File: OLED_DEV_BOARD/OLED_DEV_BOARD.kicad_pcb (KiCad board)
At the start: 2 copper layers, 32 parts, among them J1 Barrel_Jack, J2 Conn_02x10_Odd_Even, J3 AudioJack3_Ground, J4 Conn_02x20_Odd_Even, SW1 SW_DIP_x02, SW2 SW_MEC_5E, SW3 SW_MEC_5E, SW4 SW_MEC_5E, SW5 SW_MEC_5E, SW6 SW_MEC_5E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

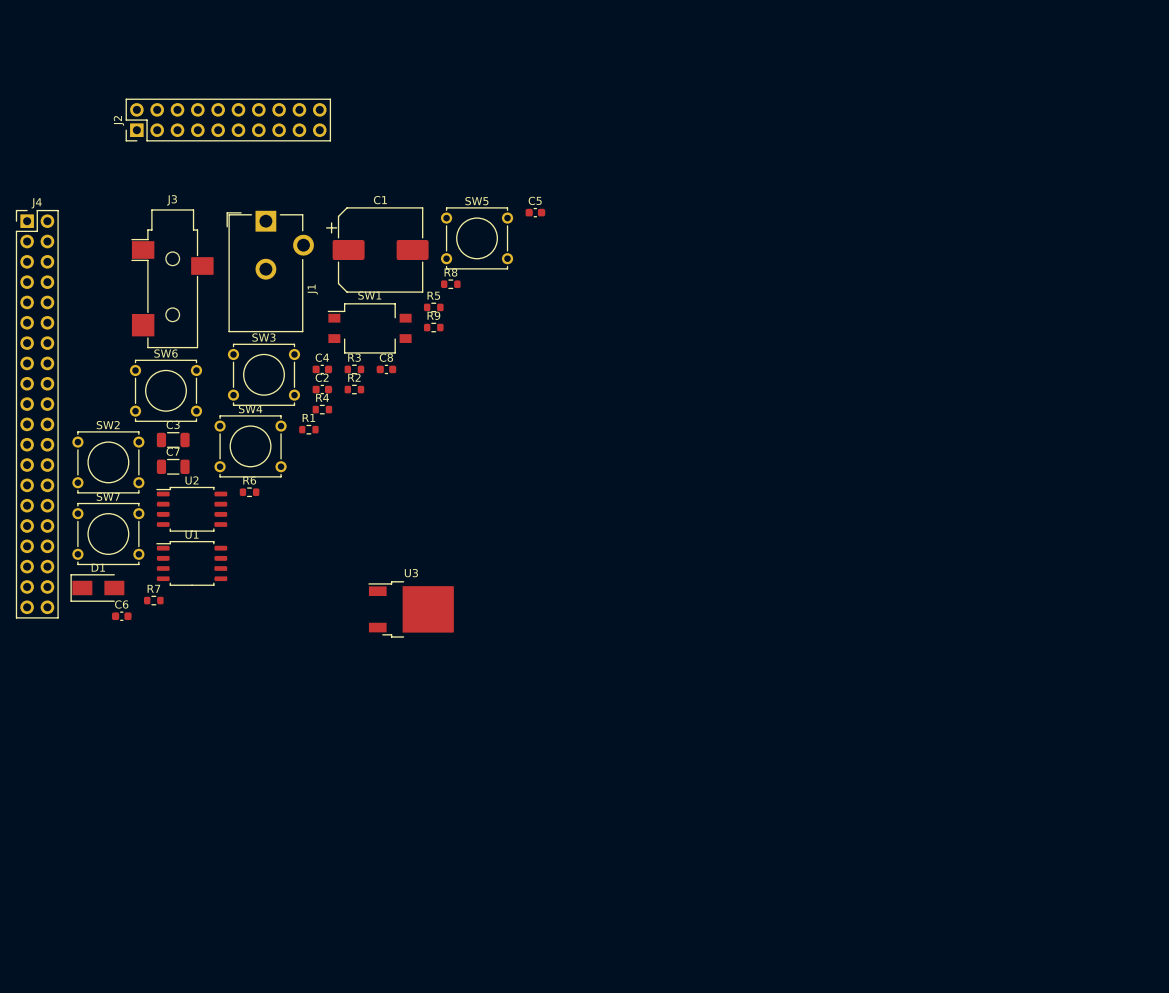
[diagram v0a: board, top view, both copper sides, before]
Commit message: Added proper footprint for OLED module and placed components roughly
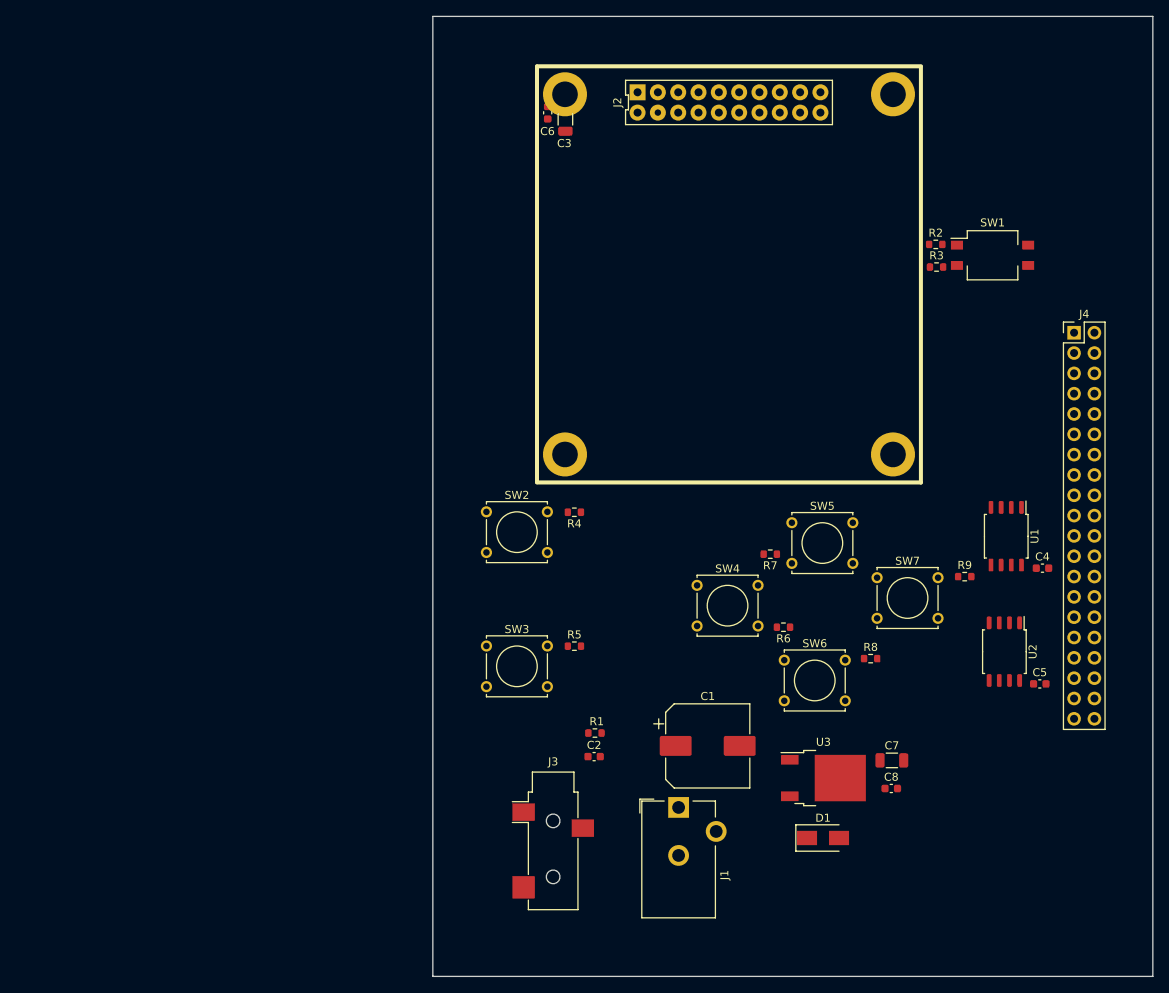
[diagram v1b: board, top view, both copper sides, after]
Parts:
- J2: footprint Connector_PinHeader_2.54mm:PinHeader_2x10_P2.54mm_Vertical -> OLED:NHD-1.8-160128UBC3
- moved J4 131.6 mm to (185.2, 69.5)
- moved U2 103.1 mm to (176.4, 109.4), turned to -90 degrees
- moved U1 101.8 mm to (176.7, 95.0), turned to -90 degrees
- moved SW7 100.2 mm to (160.5, 100.2)
- moved C7 97.0 mm to (162.4, 123.0)
- moved D1 95.8 mm to (153.8, 132.7)
- moved C4 93.4 mm to (181.2, 99.0)
- moved J1 89.6 mm to (135.7, 128.9)
- moved SW6 88.8 mm to (148.9, 110.5)
- moved C5 86.3 mm to (180.9, 113.4)
- moved J3 84.8 mm to (120.0, 133.1)
- moved C6 82.4 mm to (119.4, 42.0), turned to -90 degrees
- moved C8 82.0 mm to (162.3, 126.5)
- moved SW1 78.4 mm to (175.0, 59.9)
- moved R7 77.3 mm to (147.2, 97.2), turned to 180 degrees
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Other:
- board outline added: 90 x 120 mm

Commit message: Made board smaller
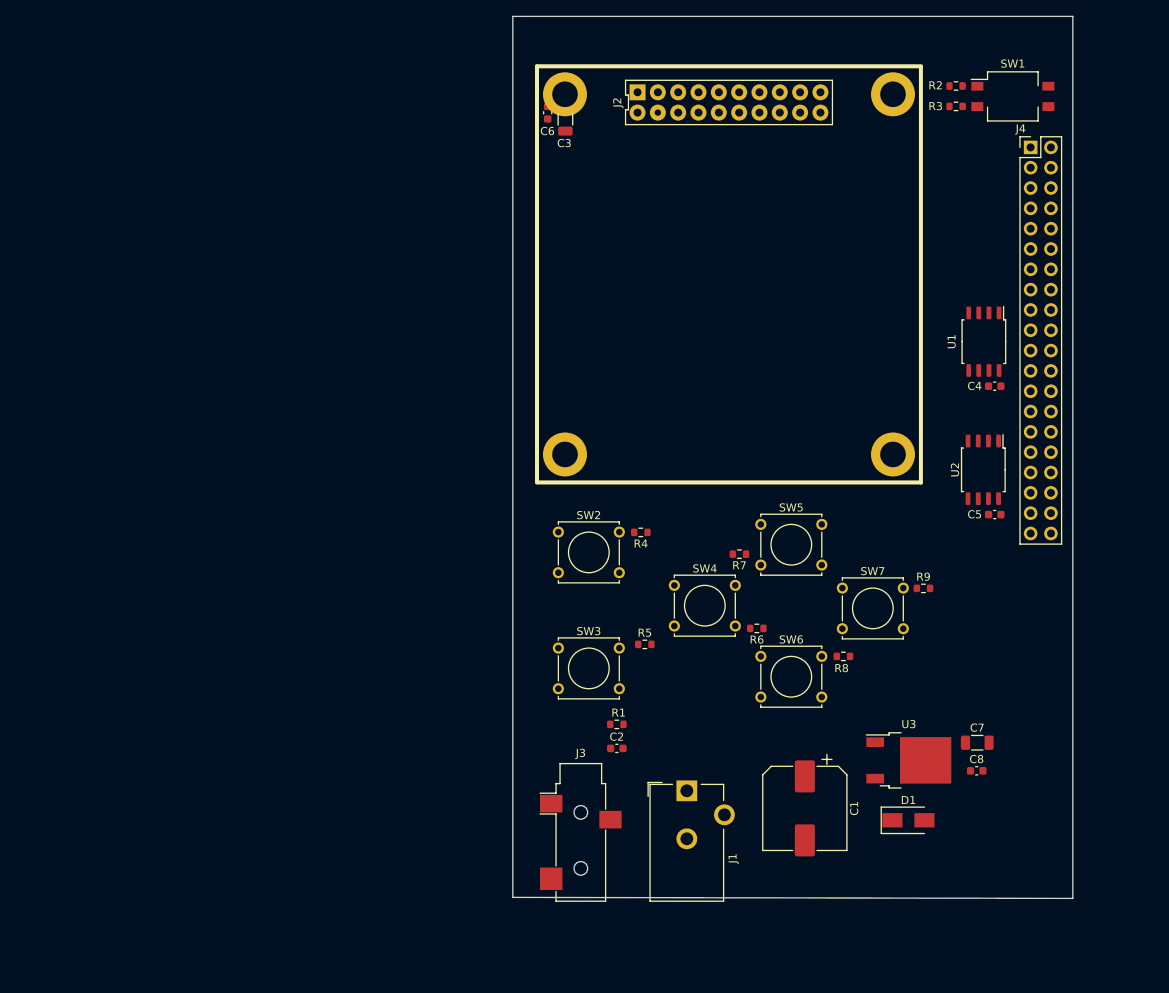
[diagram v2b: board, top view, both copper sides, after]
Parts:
- moved U1 24.5 mm to (173.9, 70.7)
- moved J4 23.8 mm to (179.7, 46.4)
- moved C4 23.5 mm to (175.2, 76.2), turned to 180 degrees
- moved U2 22.9 mm to (173.8, 86.7)
- moved C5 21.9 mm to (175.2, 92.3), turned to 180 degrees
- moved R3 20.2 mm to (170.4, 41.2)
- moved SW1 20.0 mm to (177.5, 40.0)
- moved R2 20.0 mm to (170.4, 38.7)
- moved C1 14.4 mm to (151.5, 129.0), turned to -90 degrees
- moved C8 10.9 mm to (173.0, 124.3)
- moved C7 10.9 mm to (173.1, 120.8)
- moved U3 10.9 mm to (164.5, 123.0)
- moved D1 10.9 mm to (164.4, 130.5)
- moved SW2 9.34 mm to (120.7, 94.5)
- moved SW3 8.99 mm to (120.7, 109.0)
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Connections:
- J4 pad 19: /PSRAM_CSb -> /PSRAM_D1
- J4 pad 20: /PSRAM_CLK -> /PSRAM_CSb
- J4 pad 22: /PSRAM_D1 -> /PSRAM_D2
- J4 pad 23: /PSRAM_D2 -> /PSRAM_D3
- J4 pad 24: /PSRAM_D3 -> /PSRAM_CLK
- J4 pad 31: /FLASH_CSb -> /FLASH_D1
- J4 pad 32: /FLASH_CLK -> /FLASH_CSb
- J4 pad 34: /FLASH_D1 -> /FLASH_D2
- J4 pad 35: /FLASH_D2 -> /FLASH_D3
- J4 pad 36: /FLASH_D3 -> /FLASH_CLK
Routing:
- net /PSRAM_D3: track 0.00 -> 0.76 mm
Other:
- board size 90 x 120 mm -> 70 x 110.2 mm

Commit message: Changed ordering of pins for display so it would route better
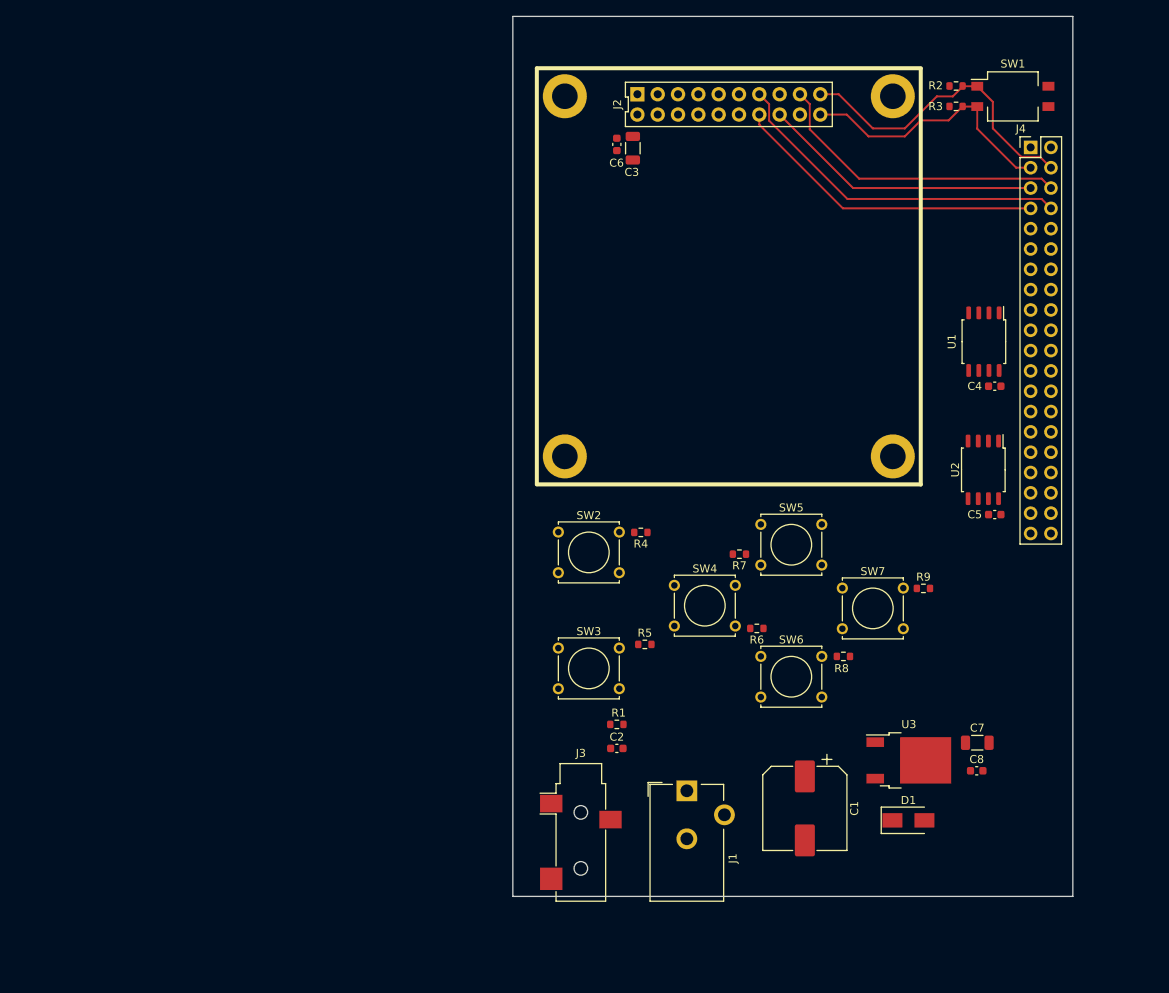
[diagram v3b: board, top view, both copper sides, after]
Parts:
- moved C6 9.50 mm to (128.0, 46.0)
- moved C3 9.17 mm to (130.0, 46.5)
- moved J2 0.24 mm to (142.0, 41.0)
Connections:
- J4 pad 10: /DB3 -> /DB4
- J4 pad 11: /DB4 -> /DB3
- J4 pad 12: /DB5 -> /DB2
- J4 pad 13: /DB6 -> /DB1
- J4 pad 14: /DB7 -> /DB0
- J4 pad 15: /RES# -> /E
- J4 pad 16: /CS# -> /R/W#
- J4 pad 17: /BS1 -> /PWM
- J4 pad 18: /BS2 -> /D/C#
- J4 pad 3: /D/C# -> /BS2
- J4 pad 4: /R/W# -> /BS1
- J4 pad 5: /E -> /RES#
- J4 pad 6: /PWM -> /CS#
- J4 pad 7: /DB0 -> /DB7
- J4 pad 8: /DB1 -> /DB6
- J4 pad 9: /DB2 -> /DB5
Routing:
- net /DB6: track 0.00 -> 43.6 mm
- net /DB7: track 0.00 -> 39.5 mm
- net /BS1: track 0.00 -> 39.0 mm
- net /CS#: track 0.00 -> 38.1 mm
- net /RES#: track 0.00 -> 35.2 mm
- net /BS2: track 0.00 -> 33.8 mm
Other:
- board size 70 x 110.2 mm -> 70 x 110 mm

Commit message: Mostly routed
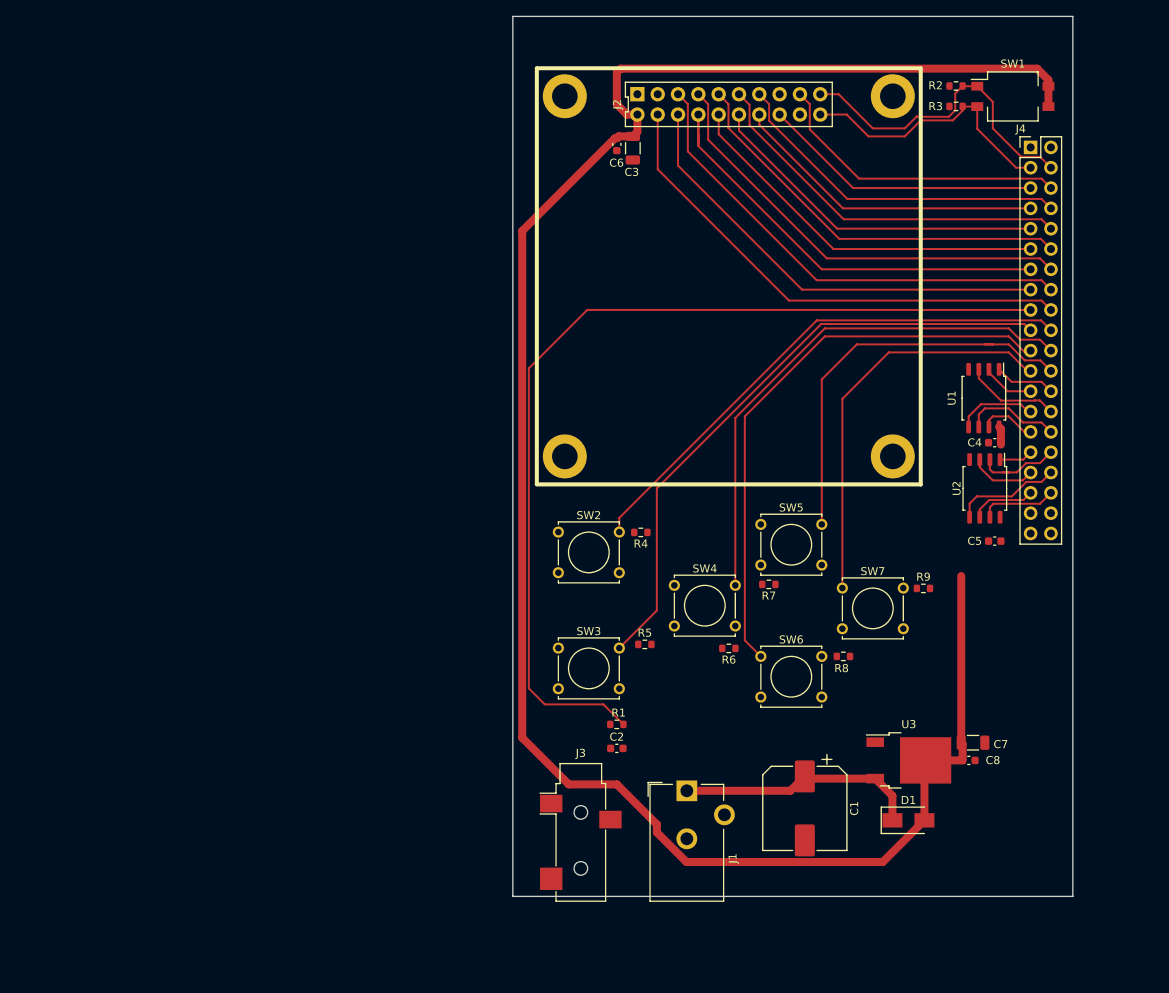
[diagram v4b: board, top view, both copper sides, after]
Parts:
- moved C4 7.06 mm to (175.2, 83.3)
- moved U1 7.06 mm to (173.9, 77.7)
- moved R7 5.27 mm to (147.0, 101.0)
- moved R6 4.30 mm to (142.0, 109.0)
- moved C5 3.32 mm to (175.2, 95.6)
- moved U2 2.33 mm to (174.0, 89.0)
- moved C8 1.63 mm to (172.0, 123.0)
- moved C7 0.53 mm to (172.5, 120.8)
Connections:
- J4 pad 19: /PSRAM_D1 -> /B_BUTTON
- J4 pad 20: /PSRAM_CSb -> /A_BUTTON
- J4 pad 21: /PSRAM_D0 -> /DOWN_BUTTON
- J4 pad 22: /PSRAM_D2 -> /LEFT_BUTTON
- J4 pad 23: /PSRAM_D3 -> /RIGHT_BUTTON
- J4 pad 24: /PSRAM_CLK -> /UP_BUTTON
- J4 pad 25: /A_BUTTON -> /PSRAM_D1
- J4 pad 26: /B_BUTTON -> /PSRAM_CSb
- J4 pad 27: /LEFT_BUTTON -> /PSRAM_D0
- J4 pad 28: /DOWN_BUTTON -> /PSRAM_D2
- J4 pad 29: /UP_BUTTON -> /PSRAM_D3
- J4 pad 30: /RIGHT_BUTTON -> /PSRAM_CLK
- J4 pad 31: /FLASH_D1 -> /FLASH_CSb
- J4 pad 32: /FLASH_CSb -> /FLASH_D1
- J4 pad 33: /FLASH_D0 -> /FLASH_D2
- J4 pad 34: /FLASH_D2 -> /FLASH_D0
- J4 pad 35: /FLASH_D3 -> /FLASH_CLK
- J4 pad 36: /FLASH_CLK -> /FLASH_D3
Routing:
- net +3V3: track 0.00 -> 249.7 mm
- net /PWM: track 0.00 -> 119.4 mm
- net /B_BUTTON: track 0.00 -> 77.5 mm
- net /DOWN_BUTTON: track 0.00 -> 70.8 mm
- net /A_BUTTON: track 0.00 -> 66.5 mm
- net /LEFT_BUTTON: track 0.00 -> 66.2 mm
- net /D/C#: track 0.00 -> 63.3 mm
- net /R/W#: track 0.00 -> 60.2 mm
- net /E: track 0.00 -> 56.9 mm
- net /DB1: track 0.00 -> 56.8 mm
- net /DB0: track 0.00 -> 55.8 mm
- net /DB2: track 0.00 -> 51.3 mm
- net /UP_BUTTON: track 0.00 -> 51.0 mm
- net /RIGHT_BUTTON: track 0.00 -> 50.6 mm
- net /DB4: track 0.00 -> 47.4 mm
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
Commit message: Added Fab Outputs
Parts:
- SW2, SW3, SW4, SW5, SW6, SW7: footprint Button_Switch_THT:SW_Tactile_Straight_KSA0Axx1LFTR -> OLED:SKHHAJA010
- moved R7 11.7 mm to (153.0, 91.0), turned to 0 degrees
- moved R8 11.5 mm to (145.0, 108.0)
- moved R6 10.0 mm to (142.0, 99.0), turned to 0 degrees
- moved R9 9.96 mm to (157.0, 98.0), turned to 180 degrees
- moved R5 5.70 mm to (127.0, 105.0)
- moved R4 5.32 mm to (127.0, 91.0), turned to 0 degrees
- moved SW6 5.00 mm to (150.0, 113.0)
- moved SW4 4.78 mm to (139.0, 104.0)
- moved SW3 4.77 mm to (125.0, 111.0)
- moved SW5 4.72 mm to (150.0, 96.0)
- moved SW7 4.58 mm to (160.0, 104.0)
- moved SW2 4.17 mm to (124.0, 97.0)
- moved C4 0.99 mm to (176.2, 83.3), turned to 0 degrees
- moved C5 0.97 mm to (176.0, 95.0), turned to 0 degrees
- turned J3 to 180 degrees
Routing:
- net +3V3: track 249.7 -> 407.5 mm
- net GND: track 0.00 -> 32.9 mm, vias 0 -> 20
- net Net-(C2-Pad1): track 0.00 -> 18.5 mm
- net /B_BUTTON: track 77.5 -> 87.9 mm
- net /DOWN_BUTTON: track 70.8 -> 81.1 mm
- net /A_BUTTON: track 66.5 -> 75.0 mm
- net /RIGHT_BUTTON: track 50.6 -> 57.1 mm
- net /LEFT_BUTTON: track 66.2 -> 72.7 mm
- net /UP_BUTTON: track 51.0 -> 57.0 mm
- net /FLASH_D1: track 10.8 -> 10.1 mm
- added copper zone on B.Cu, net GND
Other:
- board text added: "JRS 2025"
- board text added: "OLED DEV BOARD v1.0"
